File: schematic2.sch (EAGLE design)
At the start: 76 parts, among them IC1 AD620N, IC2 AD620N, IC3 AD620N, IC4 LM324N, IC5 LM324N, IC6 DS3231/SO

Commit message: created board file
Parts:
- removed R4, R5, R6, R7, R8, R9: 100K, Felicia_force_logger:RESISTOR_SMDR0805
- renumbered 100K to 80, C1 to C72, C10 to C91, C11 to C80, C12 to C81, C13 to C70, C14 to C71, C2 to C92, C3 to C82, C4 to C+, C5 to C-, C9 to C90, IC1 to JOY_X, IC2 to JOY_Y, IC3 to BEAM_Z, IC4 to REF, IC5 to AMP, JP2 to DPINS_1ST, JP3 to ANALOG_IN, JP4 to PWR_PINS, R$30 to R$80, R$31 to R$90, R$32 to R$70, R1 to R_AMP90, R2 to R_AMP80, R3 to R_AMP70, U$10 to IND-, U$2 to 90, U$25 to INPUT, U$26 to RESET, U$4 to 70, U$5 to DPINS_2ND, U$9 to IND+
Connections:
- removed net N$12: 80.P$3, R6.2
- removed net N$14: 90.P$3, R7.2
- removed net N$15: 70.P$3, R8.2
- removed net N$16: C82.1
- removed net N$17: 80.P$1, R4.1
- removed net N$20: 70.P$1, R9.1
- removed net N$8: 90.P$1, R5.1
- net +5V: now also 70.P$3, 80.P$3, 90.P$3; no longer R6.1, R7.1, R8.1
- net -5V: no longer R4.2, R5.2, R9.2
- net A0: now also C82.1
- net VNEG: now also 70.P$1, 80.P$1, 90.P$1

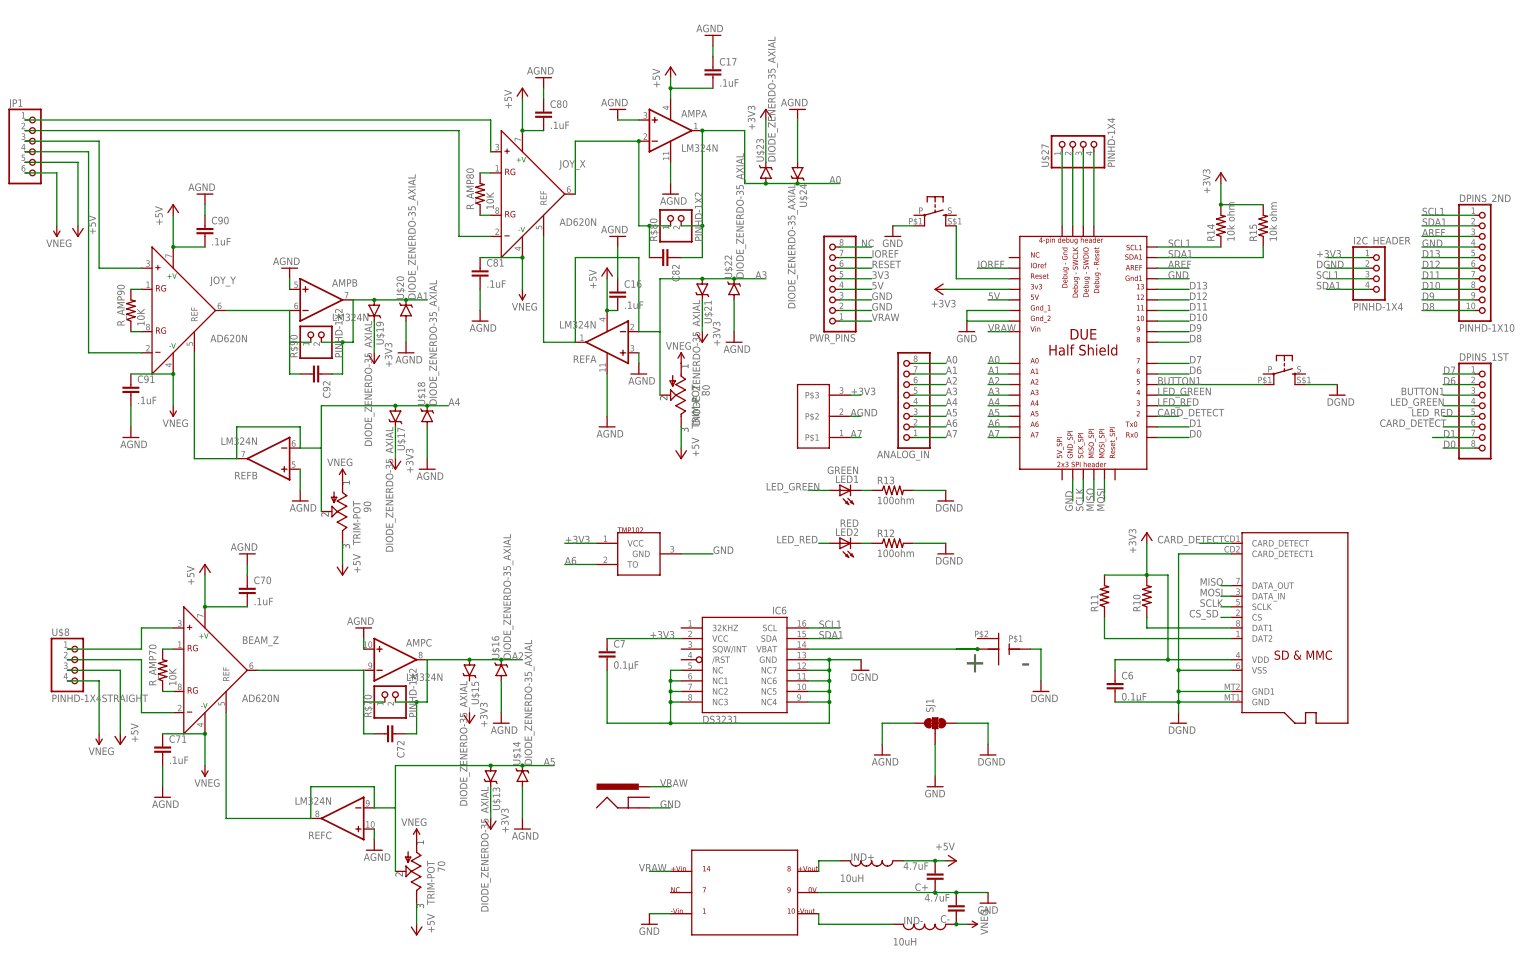
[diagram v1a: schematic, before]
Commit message: 1st complete board draft with small associated schematic changes
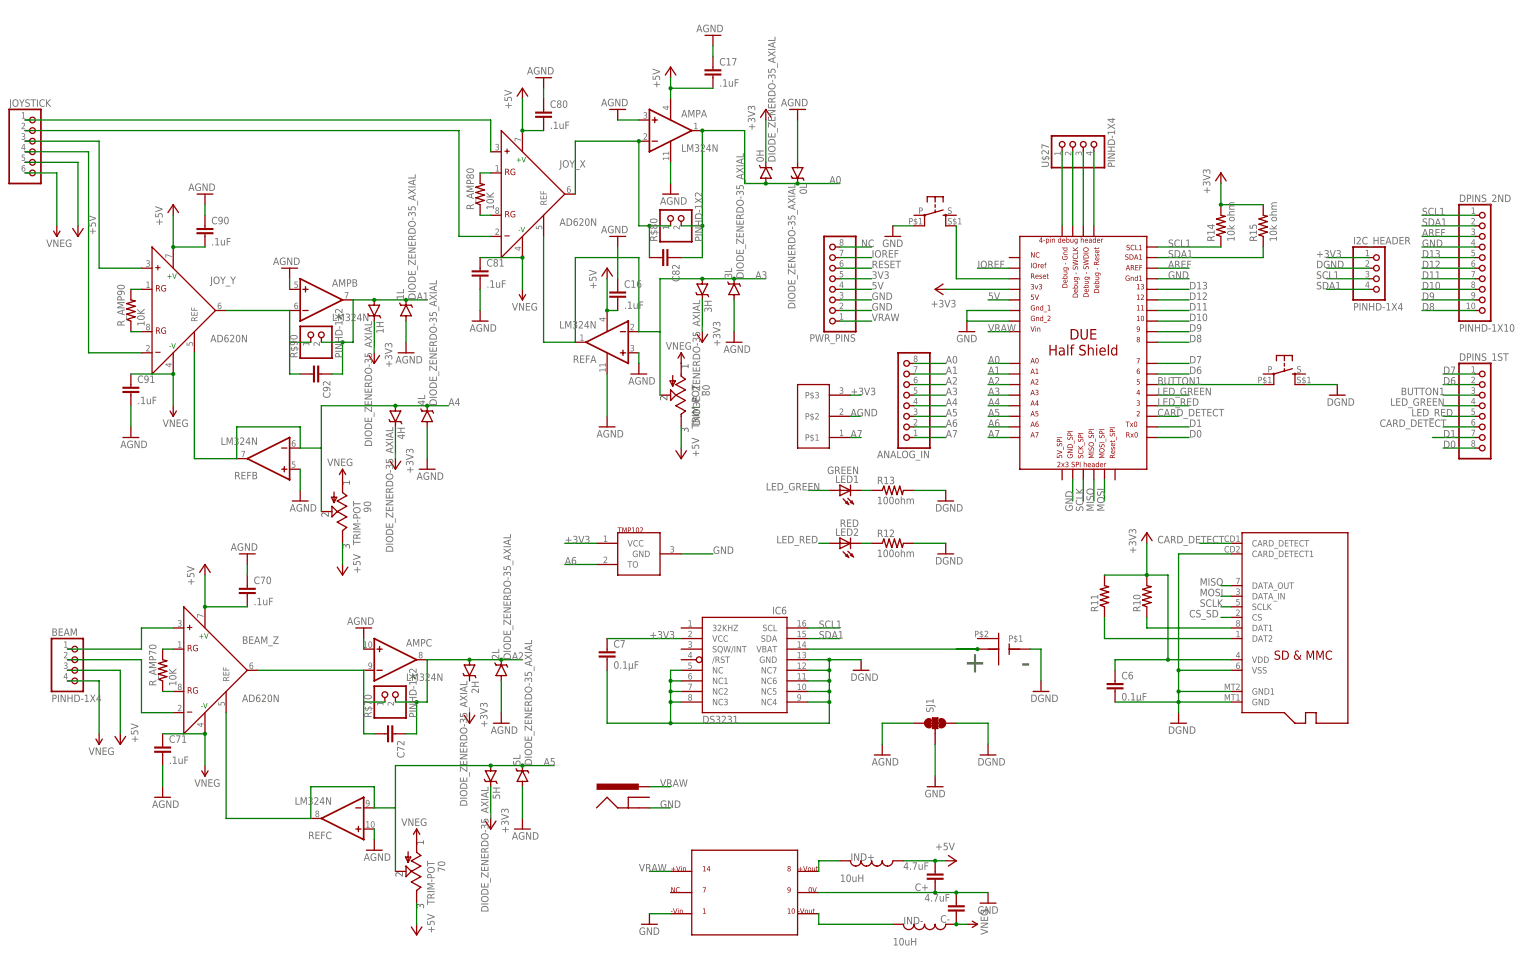
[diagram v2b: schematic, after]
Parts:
- removed U$8: PINHD-1X4STRAIGHT, Felicia_force_logger:PINHD-1X4STRAIGHT
- added BEAM: PINHD-1X4, Felicia_force_logger:PINHD-1X4
- renumbered JP1 to JOYSTICK, U$13 to 5H, U$14 to 5L, U$15 to 2H, U$16 to 2L, U$17 to 4H, U$18 to 4L, U$19 to 1H, U$20 to 1L, U$21 to 3H, U$22 to 3L, U$23 to 0H, U$24 to 0L
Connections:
- net +5V: now also BEAM.3; no longer U$8.3
- net -5V: now also BEAM.4; no longer U$8.4
- net N$31: now also BEAM.2; no longer U$8.2
- net N$32: now also BEAM.1; no longer U$8.1

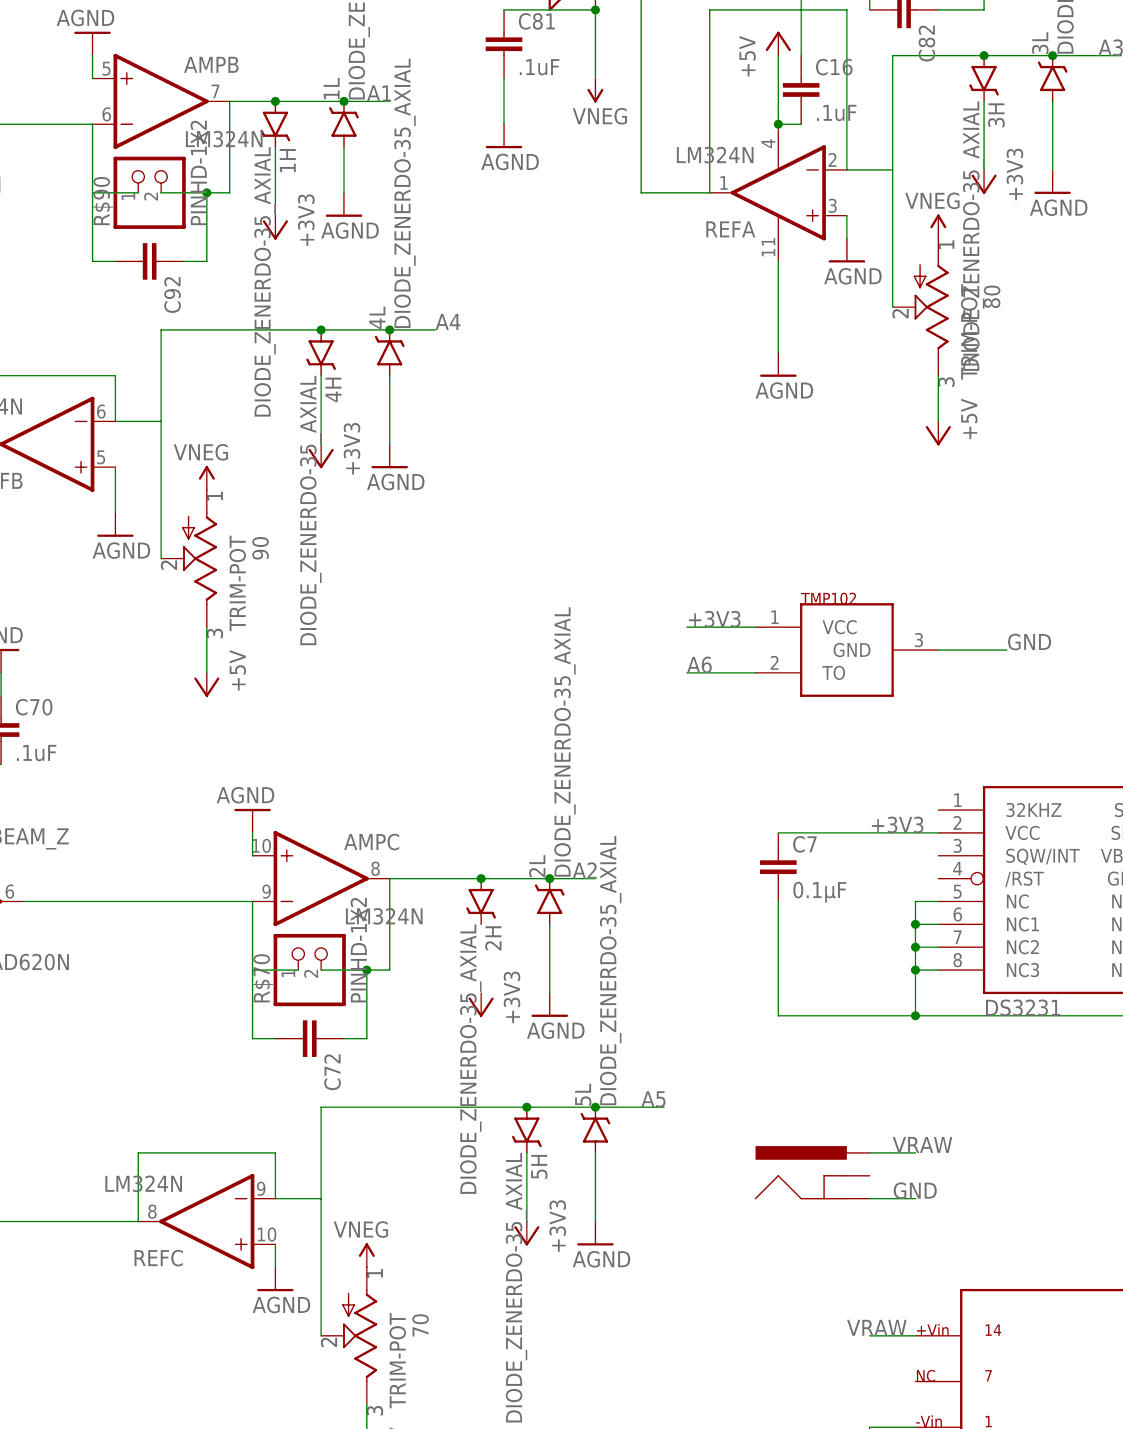
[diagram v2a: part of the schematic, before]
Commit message: Found an unconnected wire on the schematic, moved some footprints around
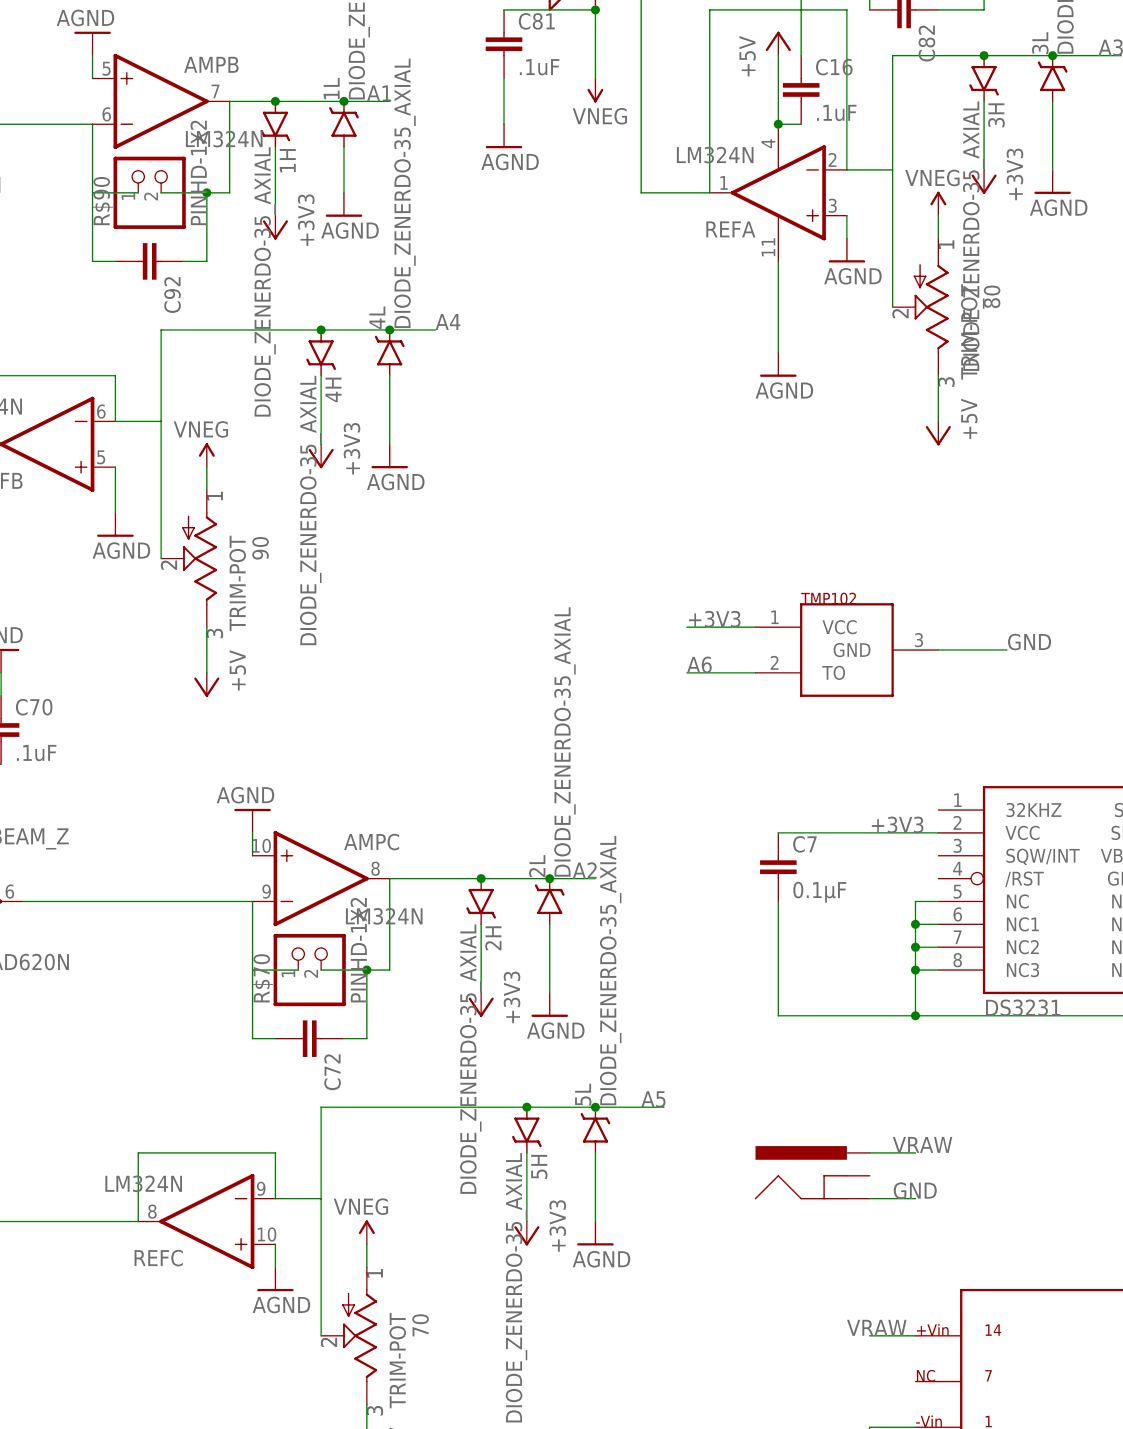
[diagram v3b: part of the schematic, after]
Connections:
- net +3V3: now also 2H.C
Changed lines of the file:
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@@
 <?xml version="1.0" encoding="utf-8"?>
 <!DOCTYPE eagle SYSTEM "eagle.dtd">
-<eagle version="7.0.0">
+<eagle version="7.2.0">
 <drawing>
 <settings>
@@
 <instance part="P-4" gate="G$2" x="116.84" y="157.48"/>
 <instance part="P+2" gate="1" x="116.84" y="208.28"/>
-<instance part="P-1" gate="G$2" x="154.94" y="144.78" rot="R180"/>
+<instance part="P-1" gate="G$2" x="154.94" y="147.32" rot="R180"/>
 <instance part="P+3" gate="1" x="154.94" y="119.38" rot="R180"/>
 <instance part="JOYSTICK" gate="A" x="0" y="193.04"/>
@@
 <instance part="P+4" gate="1" x="10.16" y="172.72" rot="R180"/>
 <instance part="P+5" gate="1" x="33.02" y="180.34"/>
-<instance part="P-7" gate="G$2" x="73.66" y="116.84" rot="R180"/>
+<instance part="P-7" gate="G$2" x="73.66" y="119.38" rot="R180"/>
 <instance part="P+6" gate="1" x="73.66" y="91.44" rot="R180"/>
-<instance part="P-8" gate="G$2" x="91.44" y="30.48" rot="R180"/>
+<instance part="P-8" gate="G$2" x="91.44" y="33.02" rot="R180"/>
 <instance part="P+7" gate="1" x="91.44" y="5.08" rot="R180"/>
 <instance part="P+8" gate="1" x="40.64" y="93.98"/>
@@
 <label x="307.34" y="167.64" size="1.778" layer="95"/>
 </segment>
+<segment>
+<pinref part="2H" gate="G$1" pin="C"/>
+<pinref part="+3V2" gate="G$1" pin="+3V3"/>
+<wire x1="104.14" y1="66.04" x2="104.14" y2="58.42" width="0.1524" layer="91"/>
+</segment>
 </net>
 <net name="N$26" class="0">
@@
 <pinref part="90" gate="G$1" pin="P$1"/>
 <pinref part="P-7" gate="G$2" pin="VNEG"/>
+<wire x1="73.66" y1="116.84" x2="73.66" y2="114.3" width="0.1524" layer="91"/>
 </segment>
 <segment>
 <pinref part="80" gate="G$1" pin="P$1"/>
 <pinref part="P-1" gate="G$2" pin="VNEG"/>
+<wire x1="154.94" y1="144.78" x2="154.94" y2="142.24" width="0.1524" layer="91"/>
 </segment>
 <segment>
 <pinref part="70" gate="G$1" pin="P$1"/>
 <pinref part="P-8" gate="G$2" pin="VNEG"/>
-</segment>
-</net>
+<wire x1="91.44" y1="30.48" x2="91.44" y2="27.94" width="0.1524" layer="91"/>
+</segment>
+</net>
